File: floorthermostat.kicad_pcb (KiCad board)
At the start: 2 copper layers, 29 parts, among them J1 Temp sensor socket 3 pin, J2 spi7segdisp, J3 Conn_01x06_Socket, J5 Programmin connector, Q1 BC549, SW1 Reset pushbutton, SW2 Enable pushbutton, U1 ESP32-WROOM-32, U2 GOLD 240V 3A SSR, U3 BD33FC0FP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

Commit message: Started designing the pcb.
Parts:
- added REF**: MountingHole_3.2mm_M3, MountingHole:MountingHole_3.2mm_M3, F.Cu at (131.0, 92.0)
- added REF**: MountingHole_3.2mm_M3, MountingHole:MountingHole_3.2mm_M3, F.Cu at (33.0, 92.0)
- added REF**: MountingHole_3.2mm_M3, MountingHole:MountingHole_3.2mm_M3, F.Cu at (47.0, 47.0)
- added REF**: MountingHole_3.2mm_M3, MountingHole:MountingHole_3.2mm_M3, F.Cu at (112.0, 85.0)
- added REF**: MountingHole_3.2mm_M3, MountingHole:MountingHole_3.2mm_M3, F.Cu at (33.0, 36.0)
- added REF**: MountingHole_3.2mm_M3, MountingHole:MountingHole_3.2mm_M3, F.Cu at (112.0, 47.0)
- added REF**: MountingHole_3.2mm_M3, MountingHole:MountingHole_3.2mm_M3, F.Cu at (47.0, 85.0)
- added REF**: MountingHole_3.2mm_M3, MountingHole:MountingHole_3.2mm_M3, F.Cu at (131.0, 36.0)
- R2, R3, R4, R5, R6, R7, R8, R9: footprint Resistor_THT:R_Axial_DIN0207_L6.3mm_D2.5mm_P2.54mm_Vertical -> Resistor_THT:R_Axial_DIN0207_L6.3mm_D2.5mm_P15.24mm_Horizontal
- moved D1 66.2 mm to (129.0, 81.0)
- moved D2 61.7 mm to (129.0, 74.0)
- moved J2 59.3 mm to (41.0, 70.5), turned to 180 degrees
- moved D3 59.2 mm to (129.0, 66.0)
- moved R1 59.1 mm to (55.0, 47.6), turned to 90 degrees
- moved D4 58.7 mm to (129.0, 58.0)
- moved R10 54.8 mm to (29.2, 48.0)
- moved R2 47.3 mm to (61.0, 72.2), turned to 90 degrees
- moved Q1 35.5 mm to (103.5, 67.0)
- moved C2 34.9 mm to (51.0, 72.0), turned to 90 degrees
- moved R9 33.1 mm to (113.0, 73.2), turned to 90 degrees
- moved C1 32.5 mm to (56.0, 72.0), turned to 90 degrees
- moved C4 32.2 mm to (120.0, 58.5), turned to -90 degrees
- moved J3 31.2 mm to (97.8, 94.0)
- moved J5 30.8 mm to (123.0, 31.9)
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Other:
- board outline added: 112 x 70 mm

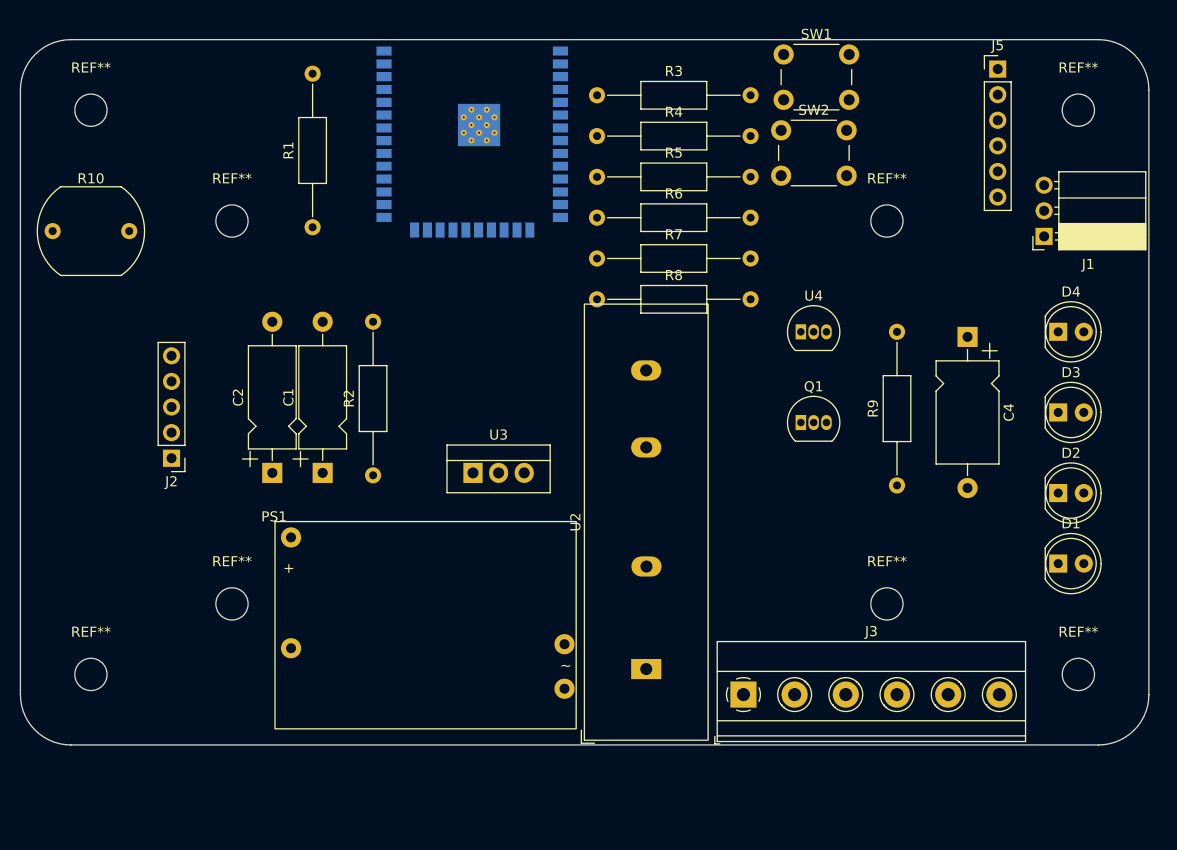
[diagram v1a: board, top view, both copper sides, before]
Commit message: Sketching component positions to pcb.
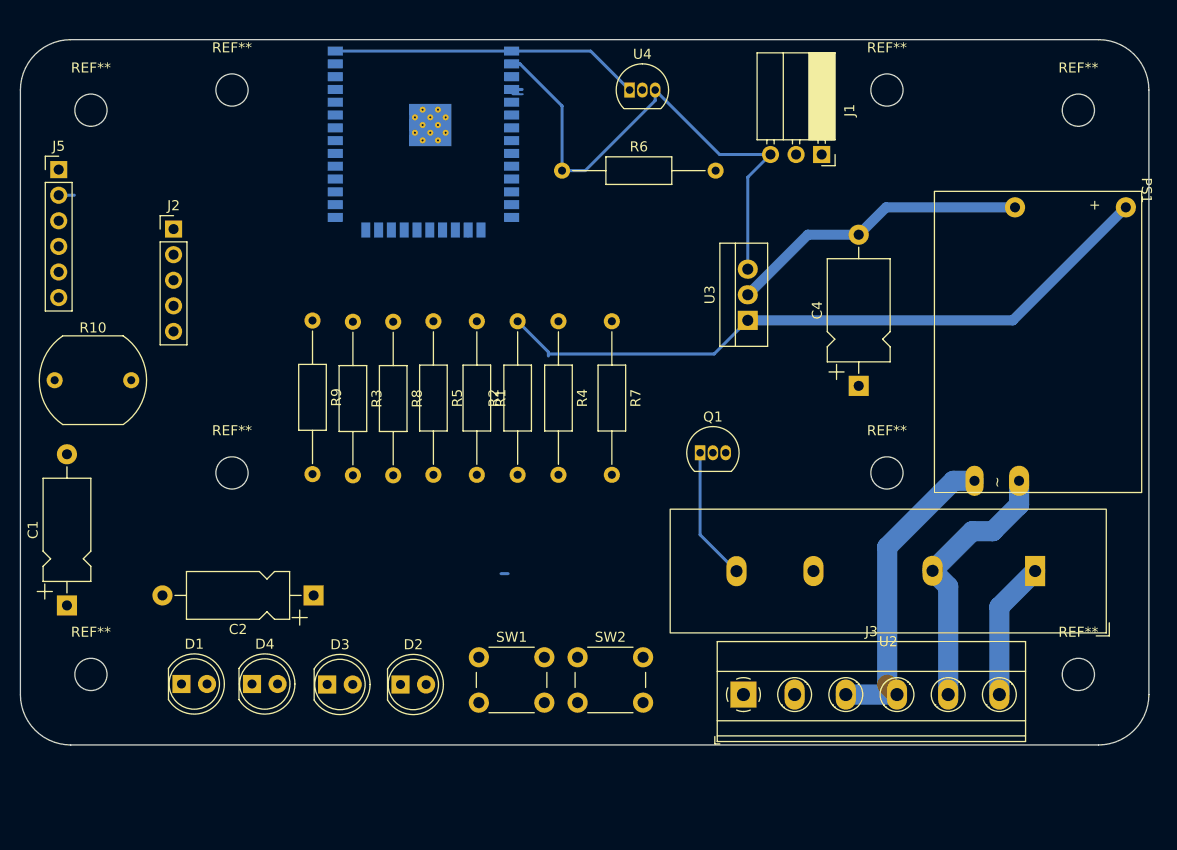
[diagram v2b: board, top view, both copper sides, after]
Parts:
- moved J5 93.7 mm to (29.8, 41.9)
- moved D1 87.8 mm to (42.0, 93.0)
- moved D4 87.3 mm to (49.0, 93.0)
- moved PS1 86.2 mm to (130.1, 45.7), turned to -90 degrees
- moved D3 77.4 mm to (56.4, 93.0)
- moved D2 68.0 mm to (63.7, 93.0)
- moved SW1 67.0 mm to (71.5, 90.3)
- moved R9 60.3 mm to (55.0, 56.9), turned to -90 degrees
- moved SW2 56.1 mm to (81.3, 90.3)
- moved U2 39.1 mm to (126.1, 81.7), turned to 180 degrees
- moved R3 33.1 mm to (59.0, 57.0), turned to -90 degrees
- moved U3 31.2 mm to (98.2, 56.9), turned to 90 degrees
- moved U4 29.4 mm to (86.5, 34.0)
- moved C1 28.6 mm to (30.6, 85.2)
- moved J1 23.5 mm to (105.5, 40.4), turned to -90 degrees
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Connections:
- J3 pad 1: /SVP -> VDD
- J3 pad 2: VDD -> /SVP
- J3 pad 3: Net-(J3-Pin_3) -> /ACN
- J3 pad 4: Net-(J3-Pin_4) -> /ACN
- J3 pad 5: Net-(J3-Pin_4) -> /ACL
- J3 pad 6: Net-(J3-Pin_6) -> /ACLO
- PS1 pad 5: Net-(J3-Pin_6) -> /ACL
- PS1 pad 6: Net-(J3-Pin_4) -> /ACN
- U2 pad 1: Net-(J3-Pin_3) -> /ACLO
- U2 pad 2: Net-(J3-Pin_4) -> /ACL
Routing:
- net +5V: track 0.00 -> 68.8 mm
- net GND: track 0.00 -> 60.9 mm
- net VDD: track 0.00 -> 52.7 mm
- net /ACN: track 0.00 -> 31.4 mm
- net /ACL: track 0.00 -> 27.0 mm
- net /ACLO: track 0.00 -> 13.7 mm
- net Net-(Q1-C): track 0.00 -> 13.2 mm
- net /SVP: track 0.00 -> 2.05 mm
- net /TX: track 0.00 -> 1.56 mm
- net /SETUP: track 0.00 -> 0.58 mm

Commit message: Changed pcb to dual-sided.
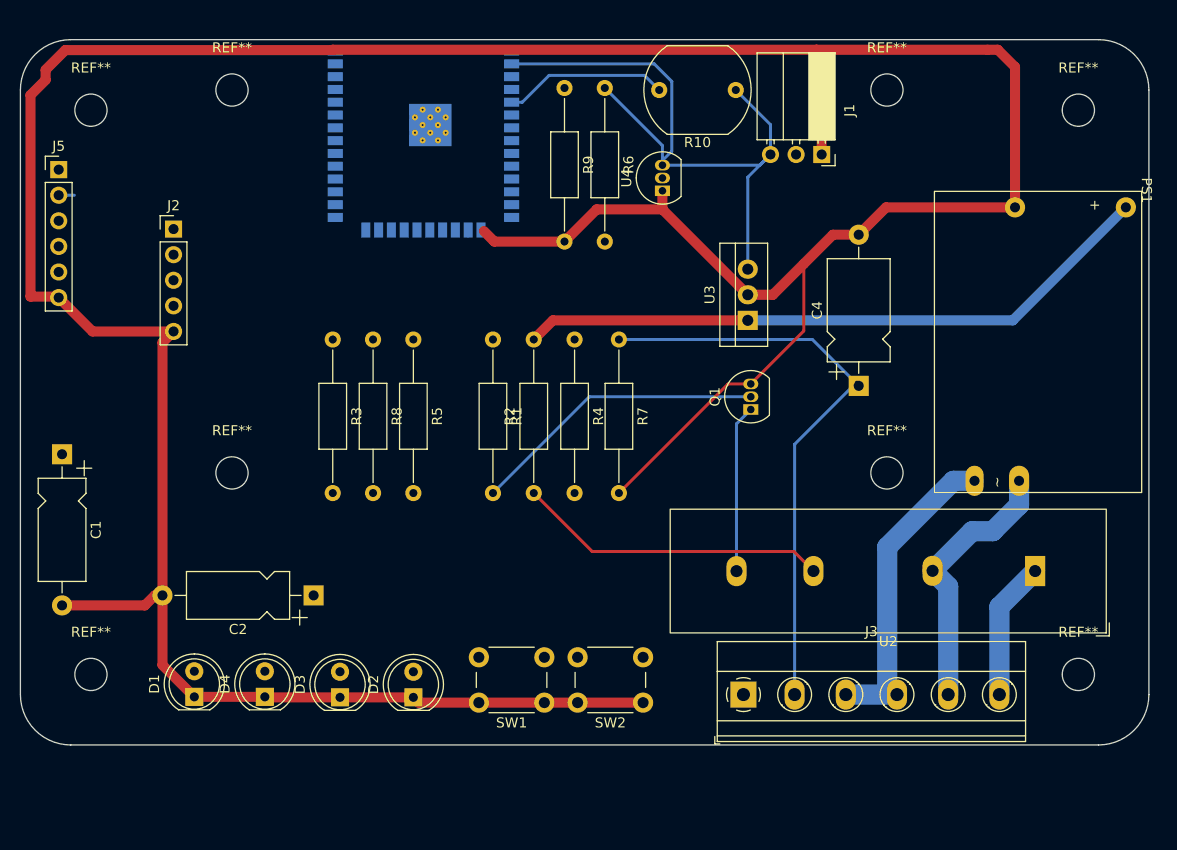
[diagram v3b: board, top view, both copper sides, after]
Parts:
- moved R10 73.5 mm to (97.0, 34.0), turned to 180 degrees
- moved R9 34.0 mm to (80.0, 33.8)
- moved C1 15.0 mm to (30.1, 70.2), turned to -90 degrees
- moved U4 10.5 mm to (89.7, 44.0), turned to 90 degrees
- moved R6 9.23 mm to (84.0, 33.8), turned to -90 degrees
- moved SW1 7.91 mm to (78.0, 94.8), turned to 180 degrees
- moved SW2 7.91 mm to (87.8, 94.8), turned to 180 degrees
- moved Q1 6.61 mm to (98.5, 65.7), turned to 90 degrees
- moved R5 2.69 mm to (65.0, 58.8)
- moved R3 2.66 mm to (57.0, 58.8)
- moved R8 2.66 mm to (61.0, 58.8)
- moved R2 2.42 mm to (77.0, 74.0)
- moved R1 2.42 mm to (72.9, 58.8)
- moved R4 2.42 mm to (81.0, 58.8)
- moved R7 1.94 mm to (85.4, 58.8)
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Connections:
- SW1 pad 2: /RESET -> /IO0
- U1 pad 16: /SETUP -> unconnected-(U1-IO13-Pad16)
- U1 pad 17: unconnected-(U1-SHD/SD2-Pad17) -> /HEATER
- U1 pad 18: unconnected-(U1-SWP/SD3-Pad18) -> /MQTT
- U1 pad 19: unconnected-(U1-SCS/CMD-Pad19) -> /MULTI
- U1 pad 20: unconnected-(U1-SCK/CLK-Pad20) -> /SETUP
- U1 pad 23: /MQTT -> unconnected-(U1-IO15-Pad23)
- U1 pad 24: /MULTI -> unconnected-(U1-IO2-Pad24)
- U1 pad 36: /HEATER -> unconnected-(U1-IO22-Pad36)
- U1 pad 37: /RESET -> unconnected-(U1-IO23-Pad37)
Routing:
- net GND: track 60.9 -> 349.5 mm
- net /SVP: track 2.05 -> 59.3 mm, vias 0 -> 1
- net Net-(R2-Pad1): track 0.00 -> 31.0 mm
- net Net-(Q1-B): track 0.00 -> 29.5 mm
- net /SVN: track 0.00 -> 16.4 mm
- net VDD: track 52.7 -> 66.2 mm
- net +5V: track 68.8 -> 64.2 mm
- net Net-(Q1-C): track 13.2 -> 16.6 mm
- net /ACN: track 31.4 -> 30.1 mm
- net unconnected-(U1-IO13-Pad16): track 0.00 -> 0.58 mm
- net /SETUP: track 0.58 -> 0.00 mm
